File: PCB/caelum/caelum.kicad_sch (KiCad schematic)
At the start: 12 parts, among them J1 BATT+, J2 BATT-, Q1 FS8205A, U1 DW01A, U2 MCP1700T-3302E

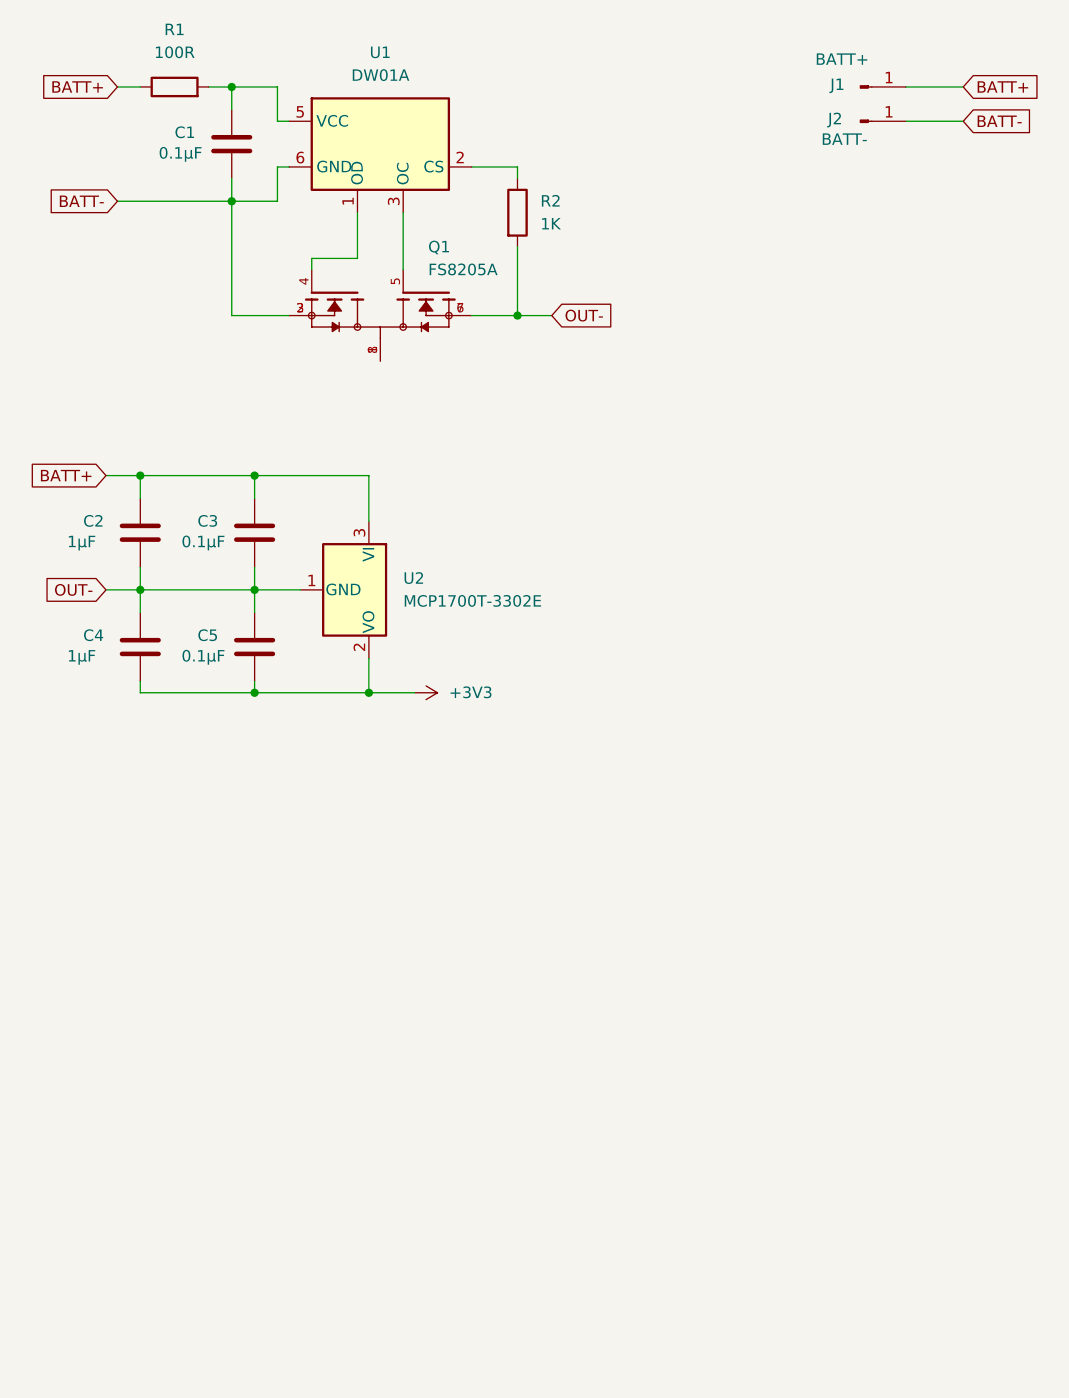
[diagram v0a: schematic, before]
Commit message: Update sdkconfig for light sleep features
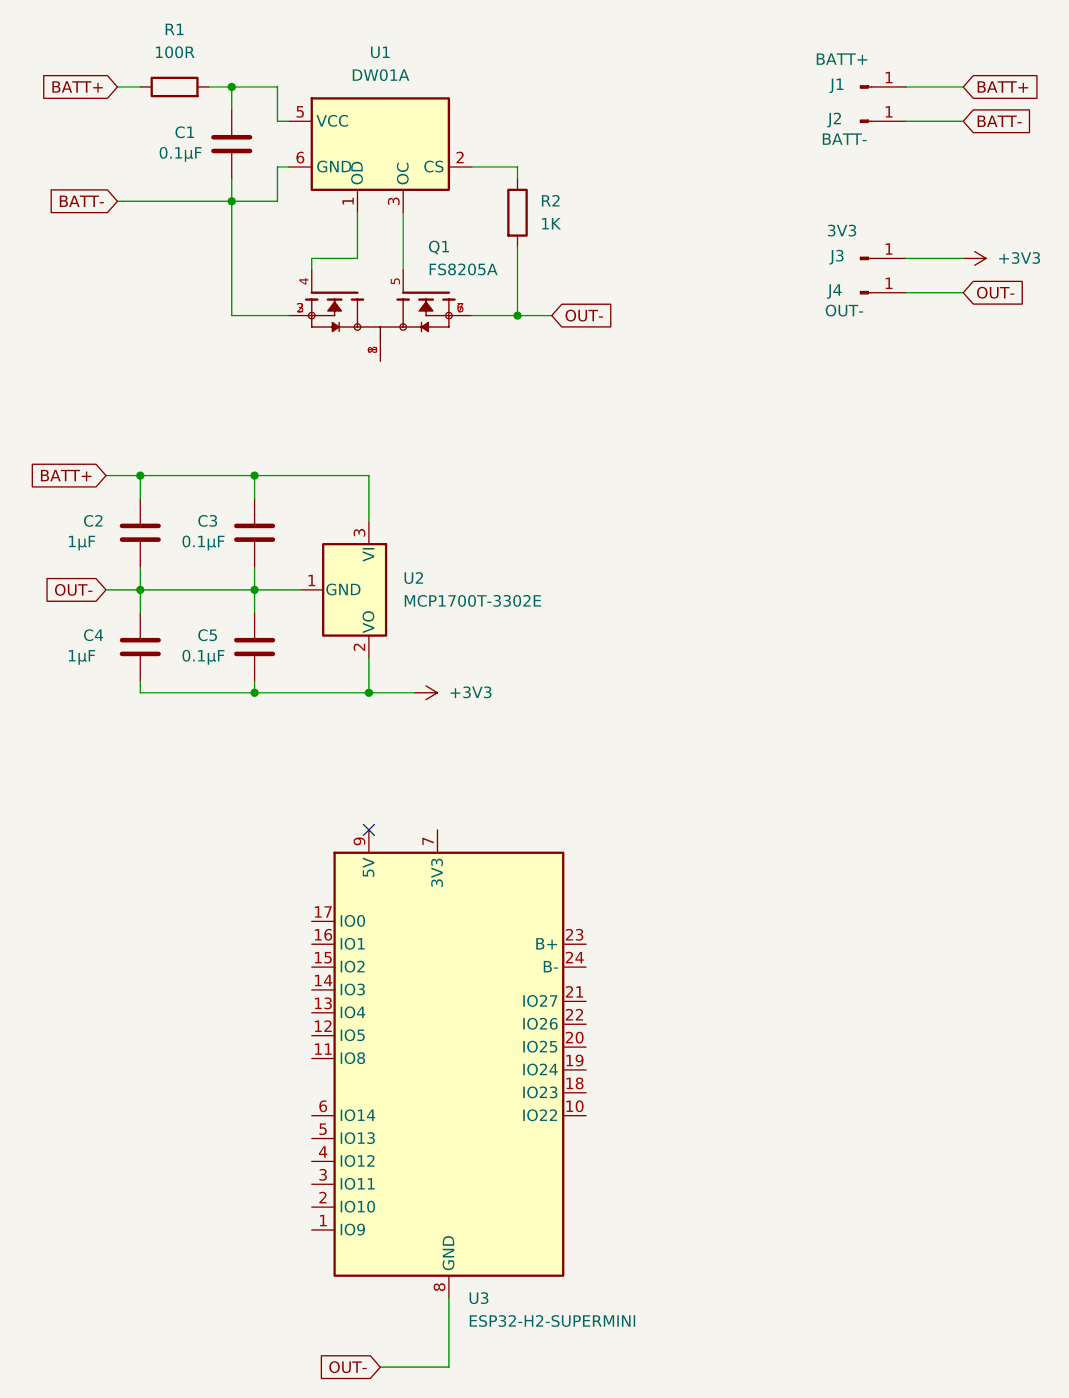
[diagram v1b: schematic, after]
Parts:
- added J3: 3V3, Connector_Pin:Pin_D1.4mm_L8.5mm_W2.8mm_FlatFork, symbol Connector:Conn_01x01_Pin
- added J4: OUT-, Connector_Pin:Pin_D1.4mm_L8.5mm_W2.8mm_FlatFork, symbol Connector:Conn_01x01_Pin
- added U3: ESP32-H2-SUPERMINI, RF_Module:ESP32-H2-SUPERMINI, symbol ESP32H2-Supermini:ESP32-S3-MINI-1
- J1, J2: footprint (none) -> Connector_Pin:Pin_D1.4mm_L8.5mm_W2.8mm_FlatFork
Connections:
- net +3V3: now also J3.1 (Pin_1)
- net OUT-: now also J4.1 (Pin_1), U3.8 (GND)
- no-connect marks 0 -> 1
